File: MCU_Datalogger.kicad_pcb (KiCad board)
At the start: 2 copper layers, 0 parts

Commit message: Setup PCBnew
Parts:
- added BT1: Battery, Connector_PinHeader_2.54mm:PinHeader_1x02_P2.54mm_Vertical, F.Cu at (132.0, 112.5)
- added C1: 0.1uF, Capacitor_SMD:C_0805_2012Metric, F.Cu at (154.3, 102.4)
- added C2: 22pF, Capacitor_SMD:C_0805_2012Metric, F.Cu at (154.3, 105.4)
- added C3: 22pF, Capacitor_SMD:C_0805_2012Metric, F.Cu at (154.3, 108.4)
- added C4: 0.1uF, Capacitor_SMD:C_0805_2012Metric, F.Cu at (154.3, 111.4)
- added C5: 100 nF, Capacitor_SMD:C_0805_2012Metric, F.Cu at (154.3, 114.5)
- added D1: LED, LED_SMD:LED_0805_2012Metric, F.Cu at (158.8, 102.4)
- added D2: LED, LED_SMD:LED_0805_2012Metric, F.Cu at (158.8, 105.5)
- added H1: MountingHole, MountingHole:MountingHole_2.1mm, F.Cu at (132.6, 90.1)
- added H2: MountingHole, MountingHole:MountingHole_2.1mm, F.Cu at (132.6, 95.8)
- added H3: MountingHole, MountingHole:MountingHole_2.1mm, F.Cu at (132.6, 101.6)
- added H4: MountingHole, MountingHole:MountingHole_2.1mm, F.Cu at (132.6, 107.3)
- added J1: Conn_01x04_Pin, Connector_PinHeader_2.54mm:PinHeader_1x04_P2.54mm_Vertical, F.Cu at (169.9, 89.5)
- added J2: Conn_01x09_Pin, Connector_PinHeader_2.54mm:PinHeader_1x09_P2.54mm_Vertical, F.Cu at (165.3, 89.5)
- added J4: Conn_02x03_Odd_Even, Connector_PinHeader_2.54mm:PinHeader_2x03_P2.54mm_Vertical, F.Cu at (169.9, 101.7)
- added J5: Conn_01x04_Pin, Connector_PinHeader_2.54mm:PinHeader_1x04_P2.54mm_Vertical, F.Cu at (174.5, 89.5)
- added R1: 10K, Resistor_SMD:R_0805_2012Metric, F.Cu at (137.7, 88.7)
- added R2: 10K, Resistor_SMD:R_0805_2012Metric, F.Cu at (137.7, 91.6)
- added R3: 4.7K, Resistor_SMD:R_0805_2012Metric, F.Cu at (137.7, 94.6)
- added R4: 4.7K, Resistor_SMD:R_0805_2012Metric, F.Cu at (137.7, 97.5)
- added R5: 330, Resistor_SMD:R_0805_2012Metric, F.Cu at (137.7, 100.5)
- added R6: 10K, Resistor_SMD:R_0805_2012Metric, F.Cu at (137.7, 103.4)
- added R7: 330, Resistor_SMD:R_0805_2012Metric, F.Cu at (137.7, 106.4)
- added U1: DS1337S_, Footprint:SOIC127P600X175-8N, F.Cu at (145.1, 115.5)
- added U2: 24LC1025, Package_SO:SOIC-8_5.3x5.3mm_P1.27mm, F.Cu at (145.1, 90.6)
- added U3: 24LC1025, Package_SO:SOIC-8_5.3x5.3mm_P1.27mm, F.Cu at (145.1, 97.5)
- added U4: ATMEGA328P-AU, Footprint:QFP80P900X900X120-32N, F.Cu at (146.4, 106.6)
- added Y1: 32.768 KHz, Crystal:Crystal_SMD_5032-2Pin_5.0x3.2mm_HandSoldering, F.Cu at (155.4, 89.8)
- added Y2: 16 MHz, Crystal:Crystal_SMD_5032-2Pin_5.0x3.2mm_HandSoldering, F.Cu at (155.4, 95.1)

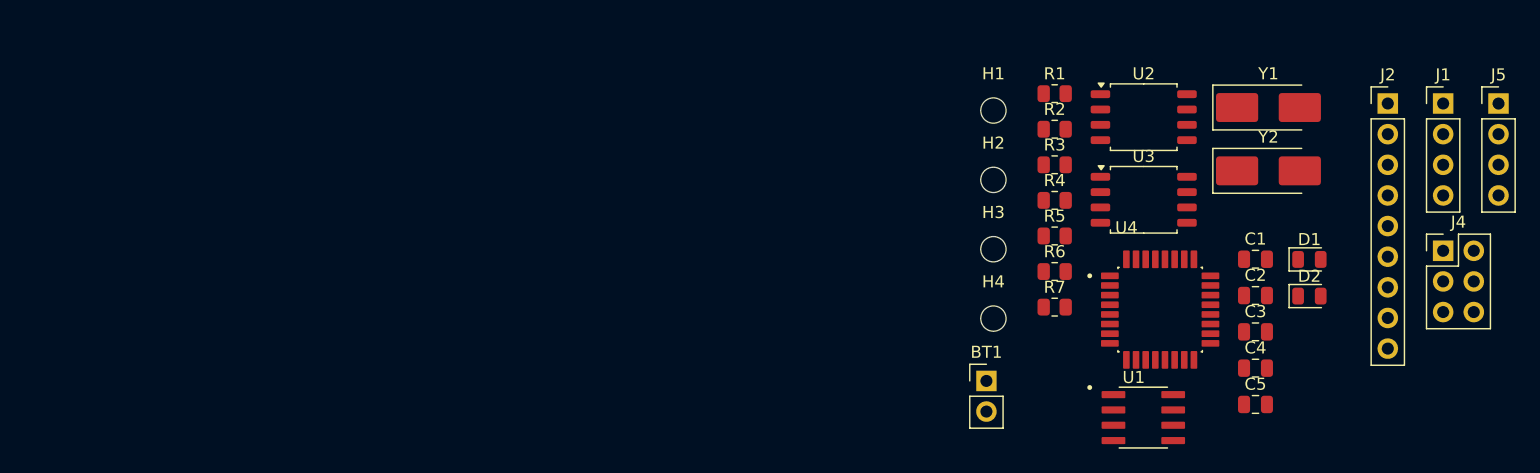
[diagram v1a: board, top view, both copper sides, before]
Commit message: Completed placement of component on pcb
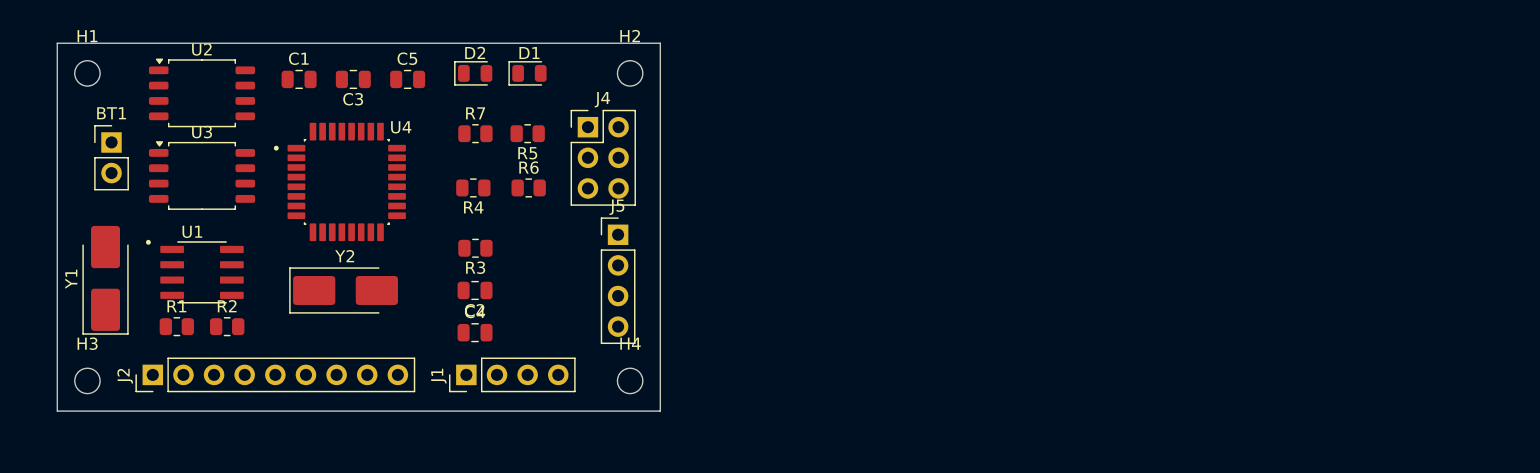
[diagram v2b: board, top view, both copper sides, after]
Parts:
- moved J2 104.8 mm to (62.9, 112.0), turned to 90 degrees
- moved Y1 97.5 mm to (59.0, 104.0), turned to 90 degrees
- moved J1 84.1 mm to (88.9, 112.0), turned to 90 degrees
- moved C1 80.7 mm to (75.0, 87.5)
- moved U1 79.0 mm to (67.0, 103.5)
- moved U2 78.1 mm to (67.0, 88.7)
- moved U3 78.1 mm to (67.0, 95.5)
- moved C3 77.7 mm to (79.5, 87.5), turned to 180 degrees
- moved Y2 77.2 mm to (78.9, 105.0)
- moved H3 75.9 mm to (57.5, 112.5)
- moved R1 75.3 mm to (64.9, 108.0)
- moved C5 75.3 mm to (84.0, 87.5)
- moved BT1 75.2 mm to (59.5, 92.7)
- moved H1 75.2 mm to (57.5, 87.0)
- moved J5 73.8 mm to (101.5, 100.4)
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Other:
- board outline added: 50 x 30.5 mm

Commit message: PCB Editing Complete
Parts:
- moved U2 7.85 mm to (67.0, 96.5)
- moved U3 6.50 mm to (67.0, 89.0)
- moved Y2 1.00 mm to (78.9, 106.0), turned to 180 degrees
- moved Y1 0.60 mm to (59.0, 104.6)
- moved R3 0.51 mm to (89.6, 101.0)
- moved U1 0.50 mm to (67.0, 103.0)
- moved R4 0.09 mm to (89.6, 96.5)
- moved R6 0.09 mm to (94.0, 96.5)
- moved R7 0.09 mm to (89.6, 92.0)
- turned R2 to 180 degrees
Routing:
- net /Vcc: track 0.00 -> 99.9 mm, vias 0 -> 1
- net /SCK: track 0.00 -> 98.4 mm, vias 0 -> 7
- net GND: track 0.00 -> 75.7 mm, vias 0 -> 10
- net /SDA: track 0.00 -> 61.5 mm, vias 0 -> 2
- net Net-(BT1-+): track 0.00 -> 55.7 mm, vias 0 -> 2
- net Net-(U4-PB7): track 0.00 -> 36.6 mm, vias 0 -> 2
- net /TX: track 0.00 -> 30.9 mm, vias 0 -> 1
- net /D2: track 0.00 -> 28.2 mm, vias 0 -> 1
- net /RX: track 0.00 -> 27.9 mm, vias 0 -> 1
- net /RESET: track 0.00 -> 26.2 mm, vias 0 -> 2
- net /MOSI: track 0.00 -> 26.1 mm
- net Net-(U4-PB6): track 0.00 -> 26.0 mm
- net /D3: track 0.00 -> 24.5 mm
- net /MISO: track 0.00 -> 22.9 mm, vias 0 -> 1
- net /D4: track 0.00 -> 21.4 mm
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- added copper zone on B.Cu, net GND
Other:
- outline, holes or cut-outs redrawn

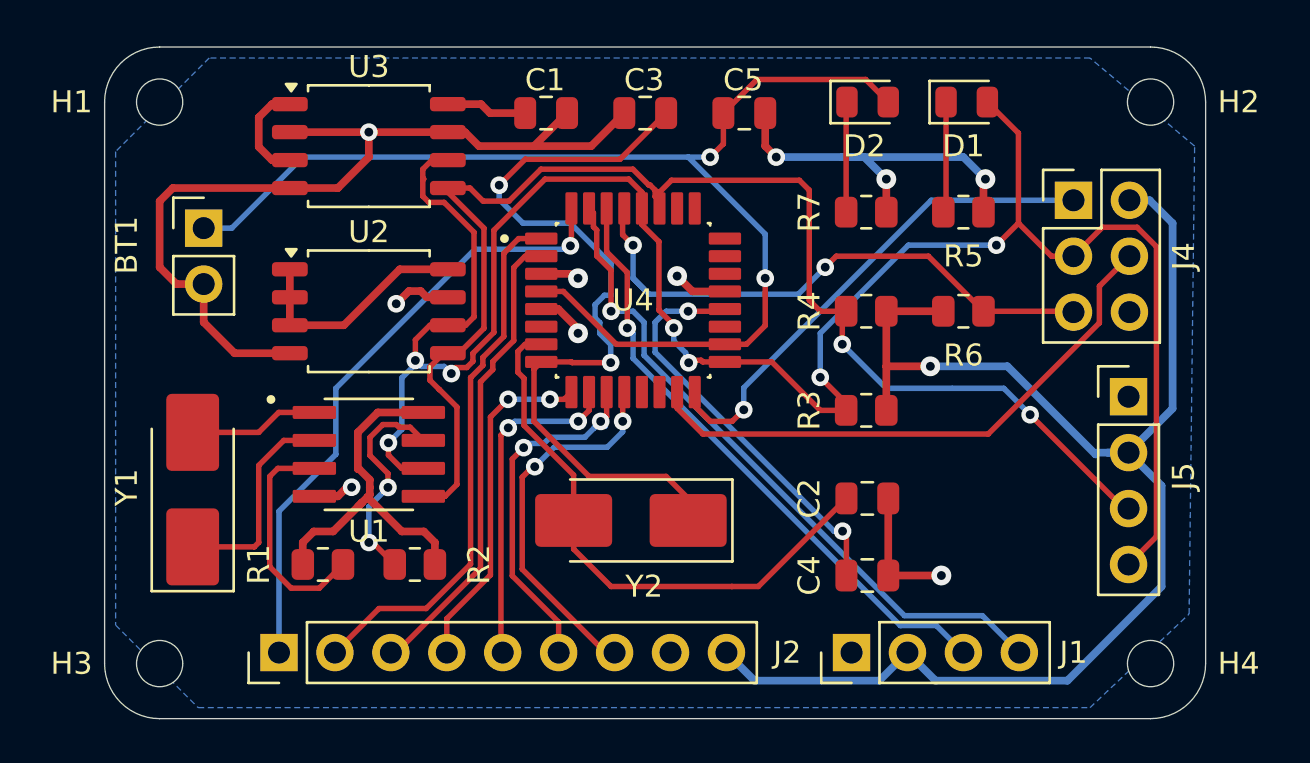
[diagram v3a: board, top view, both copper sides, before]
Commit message: 2Layer pcb done
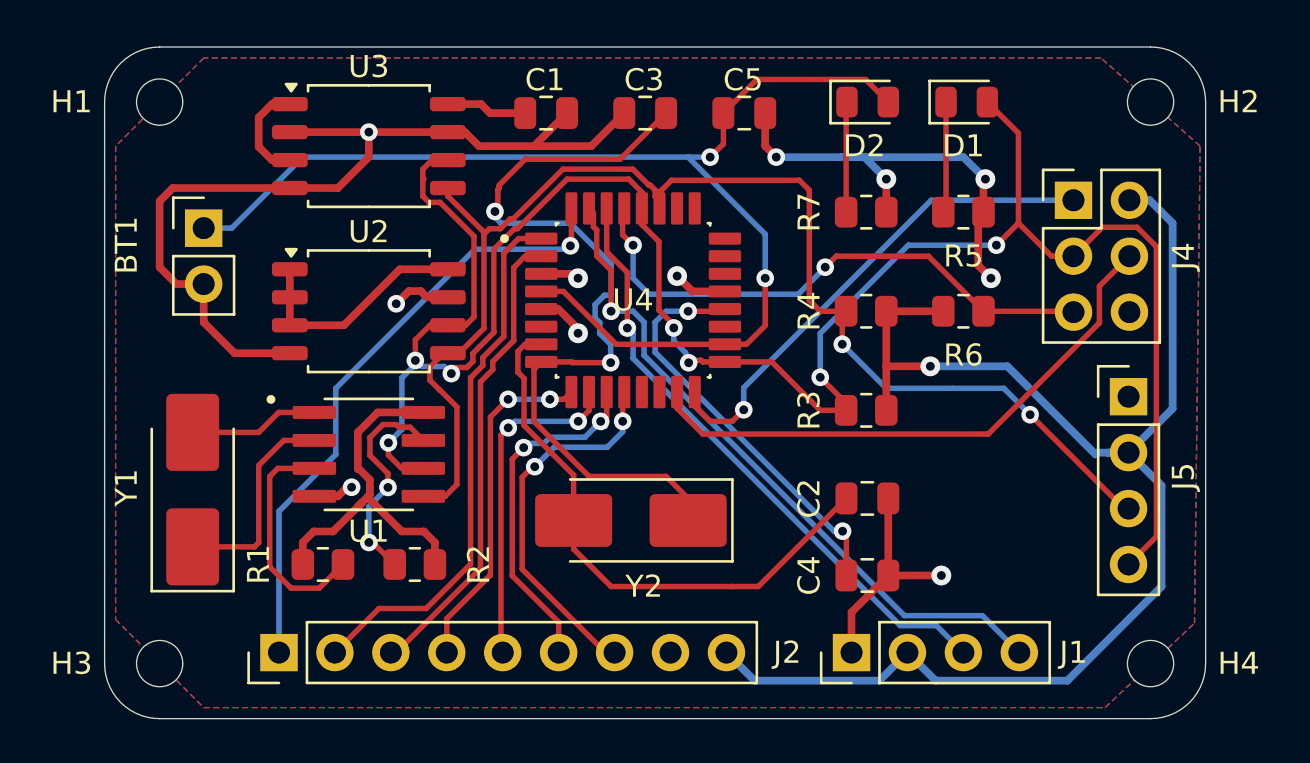
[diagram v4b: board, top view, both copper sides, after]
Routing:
- net GND: track 75.7 -> 83.2 mm, vias 10 -> 11
- net Net-(U4-PB7): track 36.6 -> 37.3 mm
- net /SDA: track 61.5 -> 60.8 mm
- net /RESET: track 26.2 -> 25.5 mm
- net /SCK: track 98.4 -> 97.8 mm
- added copper zone on F.Cu, net /Vcc
